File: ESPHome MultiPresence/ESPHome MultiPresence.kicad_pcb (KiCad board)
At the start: 2 copper layers, 31 parts, among them J1 Conn_01x06, J2 USB_C_Receptacle_Power, SW1 SW_Push, SW2 SW_Push, U1 ESP32-WROOM-32, U2 SEN0395, U3 EKMC1603113, U4 TSL2591, U5 BME280, U6 TLV75533PDBV

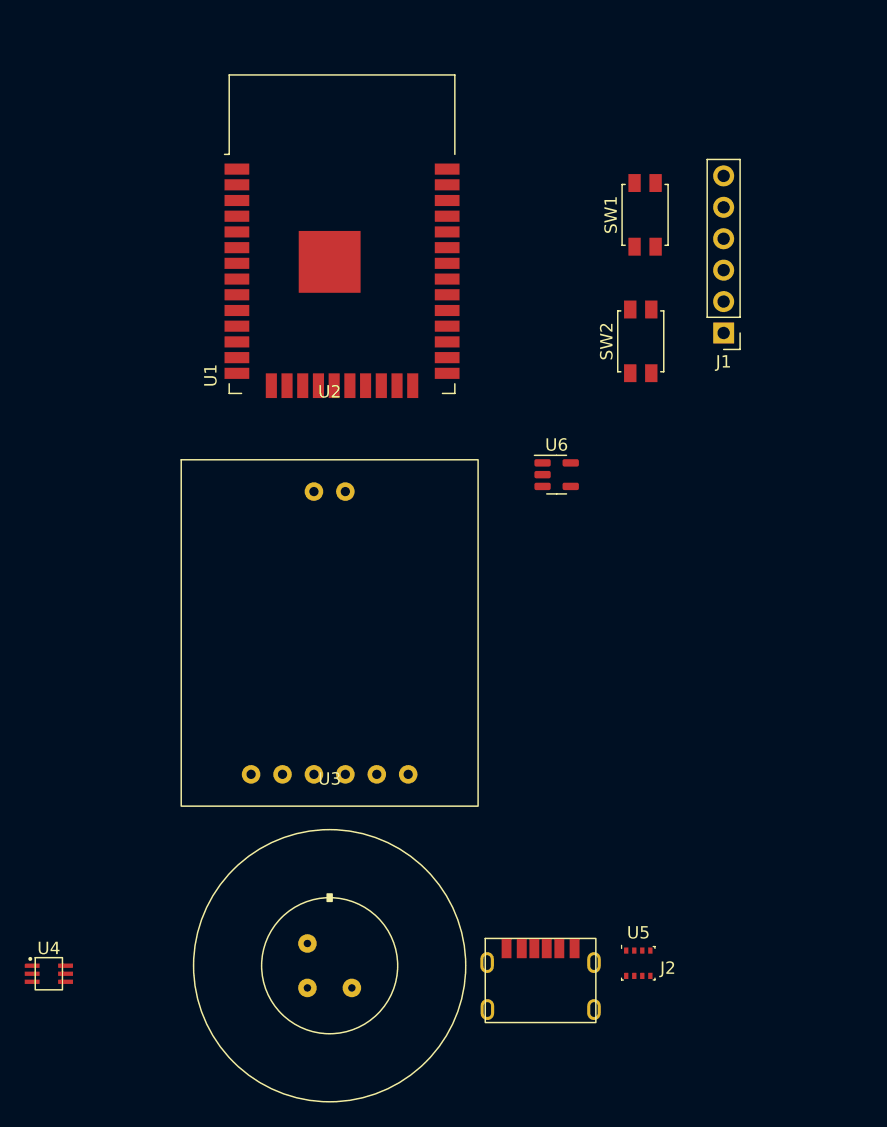
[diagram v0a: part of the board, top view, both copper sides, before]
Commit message: changed voltage switch to jumpper, changed screw terminal jst-ph
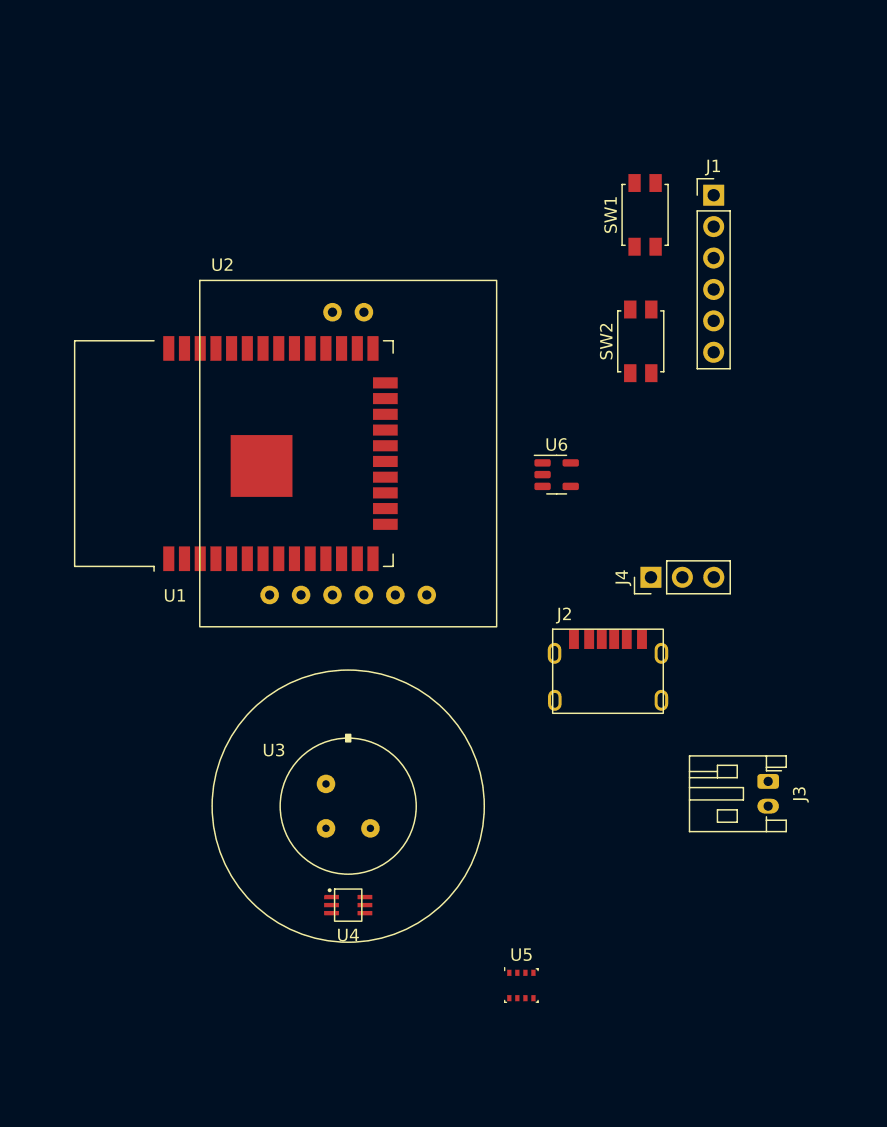
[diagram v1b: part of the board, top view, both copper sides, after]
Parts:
- added J3: Screw_Terminal_01x02, Connector_JST:JST_PH_S2B-PH-K_1x02_P2.00mm_Horizontal, F.Cu at (185.4, 102.0)
- added J4: Conn_01x03, Connector_PinHeader_2.54mm:PinHeader_1x03_P2.54mm_Vertical, F.Cu at (176.0, 85.5)
- moved J2 25.6 mm to (172.5, 89.7)
- moved U4 24.8 mm to (151.5, 112.0)
- moved U1 15.8 mm to (145.2, 75.5), turned to 90 degrees
- moved U2 14.6 mm to (151.5, 75.5)
- moved U3 13.0 mm to (151.5, 104.0)
- moved J1 11.2 mm to (181.0, 54.6), turned to 0 degrees
- moved U5 9.62 mm to (165.5, 118.5)

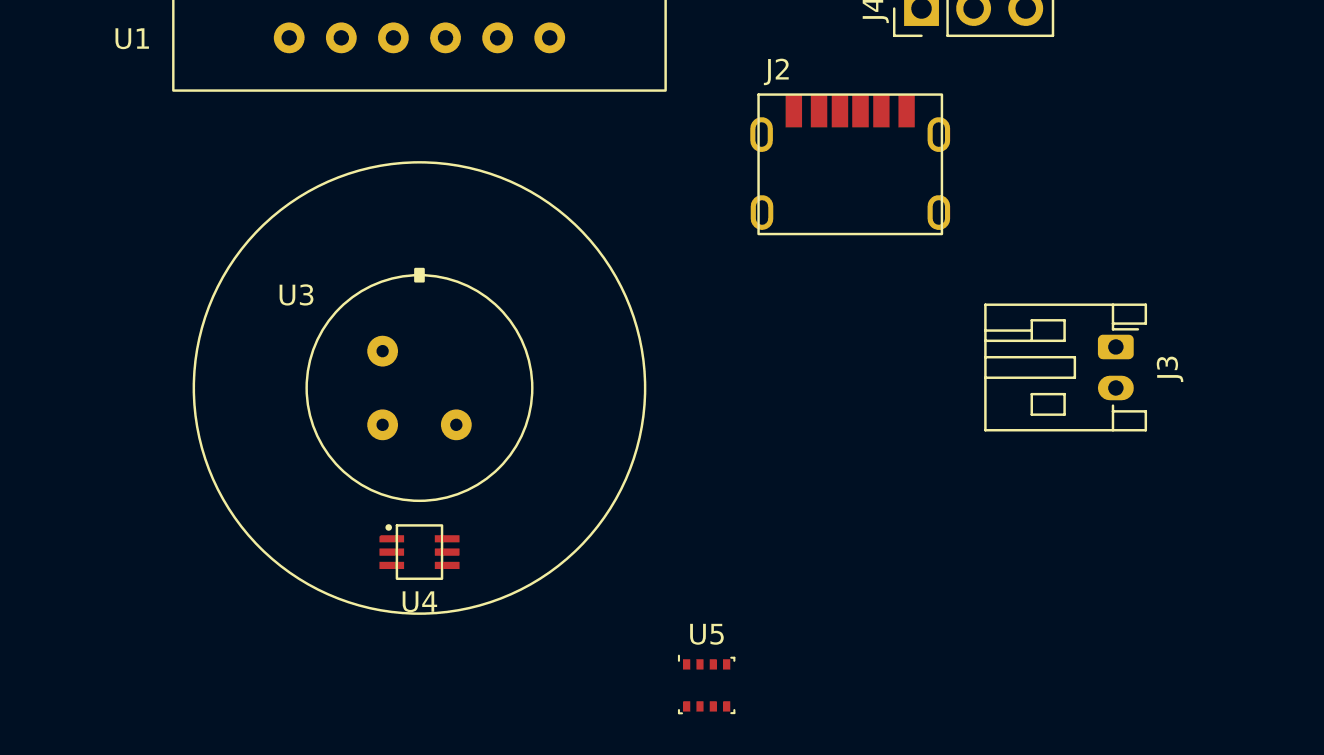
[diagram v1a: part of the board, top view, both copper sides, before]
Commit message: replaced J3 with pinheadder, fixed USB-C footprint pin assignment
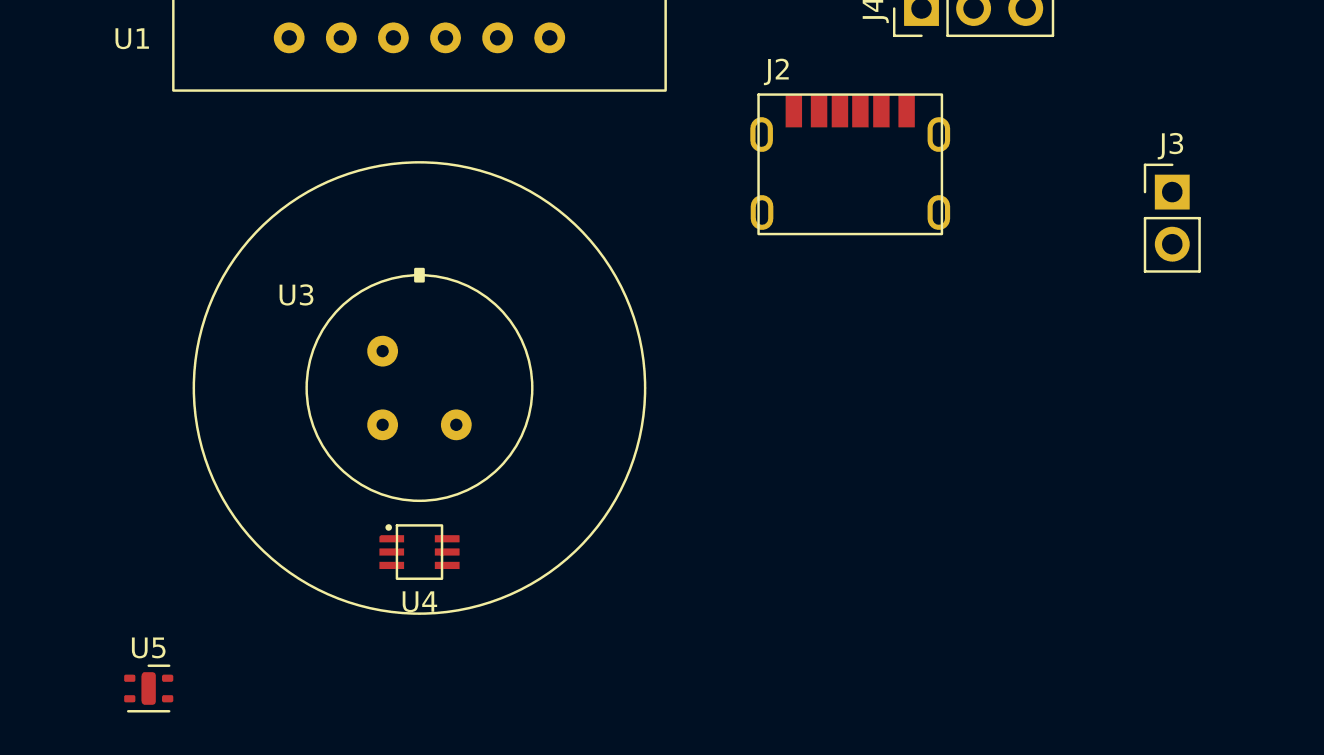
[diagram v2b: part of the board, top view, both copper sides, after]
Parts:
- J3: value Screw_Terminal_01x02 -> Conn_01x02; footprint Connector_JST:JST_PH_S2B-PH-K_1x02_P2.00mm_Horizontal -> Connector_PinHeader_2.54mm:PinHeader_1x02_P2.54mm_Vertical
- U5: value BME280 -> SHTC3; footprint Package_LGA:Bosch_LGA-8_2.5x2.5mm_P0.65mm_ClockwisePinNumbering -> Sensor_Humidity:Sensirion_DFN-4-1EP_2x2mm_P1mm_EP0.7x1.6mm
- moved U5 27.2 mm to (138.3, 118.7)
- moved J3 8.04 mm to (188.2, 94.5), turned to 0 degrees
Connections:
- U5 pad 1: GND -> +3.3V
- U5 pad 2: +3.3V -> SCL
- U5 pad 4: SCL -> GND
- U5 pad 5: GND -> unconnected-(U5-Pad5)
